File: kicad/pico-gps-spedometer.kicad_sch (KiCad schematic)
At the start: 21 parts, among them J1 Akkumulátor be, J2 TP4056-18650-Charger, J3 uBlox NEO GPS (6M/8M), Q1 PN2222A, U1 RP2040-ZERO, U2 DS18B20, U3 LM7805_TO220, U4 TFT_320x240

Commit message: Refactor code structure for improved readability and maintainability
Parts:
- added Q2: BC212, Package_TO_SOT_THT:TO-92_Inline, symbol Transistor_BJT:BC212
- added R7: 390, Resistor_THT:R_Axial_DIN0204_L3.6mm_D1.6mm_P7.62mm_Horizontal, symbol Device:R
- added R8: 4k7, Resistor_THT:R_Axial_DIN0204_L3.6mm_D1.6mm_P7.62mm_Horizontal, symbol Device:R
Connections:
- net +5VBATT: now also R7.1
- net LED: no longer names the net of U1.2 (GP1)
- net LED: now also R8.2; no longer U4.8 (LED)
- new net: Q2.2 (B), R8.1
- new net: Q2.3 (E), R7.2
- new net: Q2.1 (C), U4.8 (LED)
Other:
- moved on the sheet: R4, U4

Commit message: Refactor code structure for improved readability and maintainability
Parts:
- D1: footprint Diode_THT:D_DO-15_P15.24mm_Horizontal -> Diode_THT:D_DO-41_SOD81_P10.16mm_Horizontal
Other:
- company: (none) -> BT-Soft
- title: (none) -> Pico GPS Spedometer
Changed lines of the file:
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@@
 	(generator_version "9.0")
 	(paper "A4")
+	(title_block
+		(title "Pico GPS Spedometer")
+		(date "2025-08-16")
+		(company "BT-Soft")
+	)
 	(junction
 		(at 222.25 31.75)
@@
 			)
 		)
-		(property "Footprint" "Diode_THT:D_DO-15_P15.24mm_Horizontal"
+		(property "Footprint" "Diode_THT:D_DO-41_SOD81_P10.16mm_Horizontal"
 			(at 237.49 31.75 0)
 			(effects

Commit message: Refactor code structure for improved readability and maintainability
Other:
- note added: "A TFT SDO/MISO bekötése opcionális! Akkor kell, ha a TFT-ről pixel adatokat szeretnénk beolvasni"
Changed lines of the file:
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@@
 		(company "BT-Soft")
+	)
+	(text "A TFT SDO/MISO bekötése opcionális!\nAkkor kell, ha a TFT-ről pixel adatokat szeretnénk beolvasni"
+		(exclude_from_sim no)
+		(at 14.732 15.24 0)
+		(effects
+			(font
+				(size 1.27 1.27)
+				(thickness 0.1588)
+			)
+			(justify left)
+		)
 	)
 	(junction

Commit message: Refactor code structure and remove redundant functions for improved readability and maintainability
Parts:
- R2: value 22k -> 15k
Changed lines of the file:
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@@
 			)
 		)
-		(property "Value" "22k"
+		(property "Value" "15k"
 			(at 157.48 92.7099 0)
 			(effects

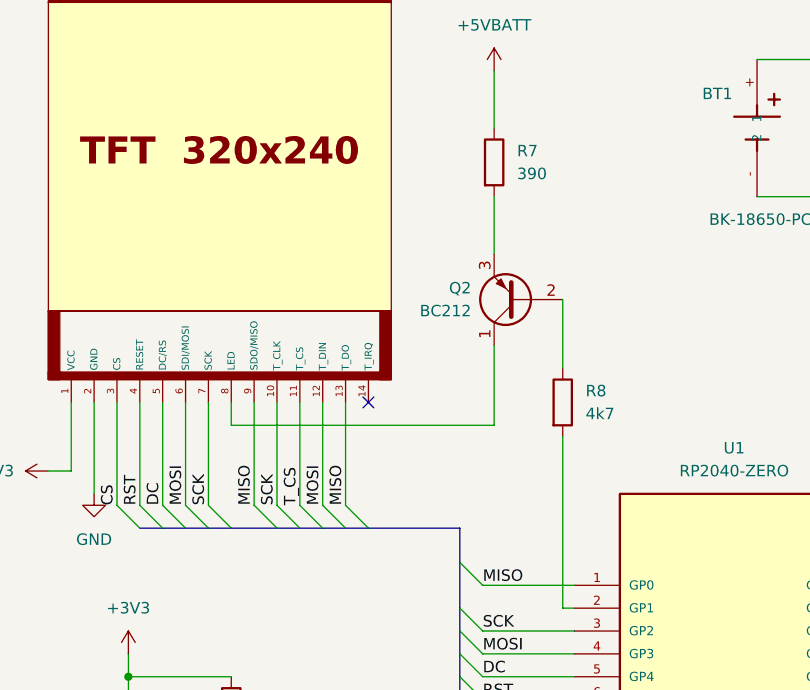
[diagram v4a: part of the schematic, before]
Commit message: Refactor TftBackLightAdjuster: Add debug log for backlight brightness adjustment
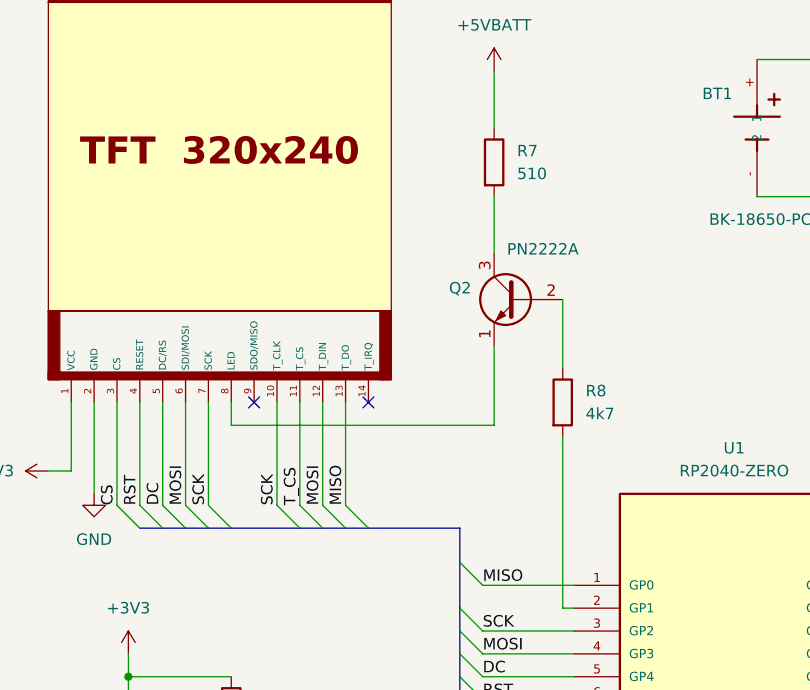
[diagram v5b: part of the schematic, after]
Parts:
- removed Q2: BC212, Package_TO_SOT_THT:TO-92_Inline, symbol Transistor_BJT:BC212
- added Q2: PN2222A, Package_TO_SOT_THT:TO-92_Inline, symbol Transistor_BJT:PN2222A
- R7: value 390 -> 510
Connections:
- net MISO: no longer U4.9 (SDO/MISO)
- net at R8.1: now also Q2.2 (B)
- net at R7.2: now also Q2.3 (C)
- net at U4.8 (LED): now also Q2.1 (E)
- no-connect marks 8 -> 9
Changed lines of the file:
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@@
 	)
 	(no_connect
+		(at 60.96 68.58)
+	)
+	(no_connect
 		(at 132.08 88.9)
 	)
@@
 	)
 	(bus_entry
-		(at 60.96 80.01)
-		(size 2.54 2.54)
-		(stroke
-			(width 0)
-			(type default)
-		)
-	)
-	(bus_entry
 		(at 83.82 96.52)
 		(size 2.54 2.54)
@@
 	(wire
 		(pts
-			(xy 60.96 68.58) (xy 60.96 80.01)
-		)
-		(stroke
-			(width 0)
-			(type default)
-		)
-	)
-	(wire
-		(pts
 			(xy 43.18 68.58) (xy 43.18 78.74)
 		)
@@
 	(bus
 		(pts
-			(xy 58.42 82.55) (xy 63.5 82.55)
+			(xy 58.42 82.55) (xy 66.04 82.55)
 		)
 		(stroke
@@
 		)
 	)
-	(bus
-		(pts
-			(xy 63.5 82.55) (xy 66.04 82.55)
-		)
-		(stroke
-			(width 0)
-			(type default)
-		)
-	)
 	(wire
 		(pts
@@
 		)
 	)
-	(label "MISO"
-		(at 60.96 80.01 90)
-		(effects
-			(font
-				(size 1.27 1.27)
-			)
-			(justify left bottom)
-		)
-	)
 	(label "CS"
 		(at 86.36 104.14 0)
@@
 			)
 		)
-		(property "Value" "390"
+		(property "Value" "510"
 			(at 90.17 43.1799 0)
 			(effects
@@
 	)
 	(symbol
-		(lib_id "Transistor_BJT:BC212")
-		(at 90.17 57.15 180)
-		(unit 1)
-		(exclude_from_sim no)
-		(in_bom yes)
-		(on_board yes)
-		(dnp no)
-		(fields_autoplaced yes)
-		(property "Reference" "Q2"
-			(at 85.09 55.8799 0)
-			(effects
-				(font
-					(size 1.27 1.27)
-				)
-				(justify left)
-			)
-		)
-		(property "Value" "BC212"
-			(at 85.09 58.4199 0)
-			(effects
-				(font
-					(size 1.27 1.27)
-				)
-				(justify left)
-			)
-		)
-		(property "Footprint" "Package_TO_SOT_THT:TO-92_Inline"
-			(at 85.09 55.245 0)
-			(effects
-				(font
-					(size 1.27 1.27)
-					(italic yes)
-				)
-				(justify left)
-				(hide yes)
-			)
-		)
-		(property "Datasheet" "https://media.digikey.com/pdf/Data%20Sheets/Fairchild%20PDFs/BC212.pdf"
-			(at 85.09 53.34 0)
-			(effects
-				(font
-					(size 1.27 1.27)
-				)
-				(justify left)
-				(hide yes)
-			)
-		)
-		(property "Description" "0.3A Ic, 50V Vce, PNP Transistor, TO-92"
-			(at 90.17 57.15 0)
-			(effects
-				(font
-					(size 1.27 1.27)
-				)
-				(hide yes)
-			)
-		)
-		(pin "1"
-		)
-		(pin "3"
-		)
-		(pin "2"
-		)
-		(instances
-			(project ""
-				(path "/33c280c0-d5d0-4346-a42c-293ed40465e2"
-					(reference "Q2")
-					(unit 1)
-				)
-			)
-		)
-	)
-	(symbol
 		(lib_id "Sensor_Temperature:DS18B20")
 		(at 46.99 109.22 0)
@@
 					(unit 1)
 				)
+			)
+		)
+	)
+	(symbol
+		(lib_id "Transistor_BJT:PN2222A")
+		(at 90.17 57.15 0)
+		(mirror y)
+		(unit 1)
+		(exclude_from_sim no)
+		(in_bom yes)
+		(on_board yes)
+		(dnp no)
+		(property "Reference" "Q2"
+			(at 85.09 55.8799 0)
+			(effects
+				(font
+					(size 1.27 1.27)
+				)
+				(justify left)
+			)
+		)
+		(property "Value" "PN2222A"
+			(at 97.028 51.562 0)
+			(effects
+				(font
+					(size 1.27 1.27)
+				)
+				(justify left)
+			)
+		)
+		(property "Footprint" "Package_TO_SOT_THT:TO-92_Inline"
+			(at 85.09 59.055 0)
+			(effects
+				(font
+					(size 1.27 1.27)
+					(italic yes)
+				)
+				(justify left)
+				(hide yes)
+			)
+		)
+		(property "Datasheet" "https://www.onsemi.com/pub/Collateral/PN2222-D.PDF"
+			(at 90.17 57.15 0)
+			(effects
+				(font
+					(size 1.27 1.27)
+				)
+				(justify left)
+				(hide yes)
+			)
+		)
+		(property "Description" "1A Ic, 40V Vce, NPN Transistor, General Purpose Transistor, TO-92"
+			(at 90.17 57.15 0)
+			(effects
+				(font
+					(size 1.27 1.27)
+				)
+				(hide yes)
+			)
+		)
+		(pin "2"
+		)
+		(pin "3"
+		)
+		(pin "1"
+		)
+		(instances
+			(project "pico-gps-spedometer"
+				(path "/33c280c0-d5d0-4346-a42c-293ed40465e2"
+					(reference "Q2")
+					(unit 1)
+				)
